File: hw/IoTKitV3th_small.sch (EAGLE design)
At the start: 13 parts

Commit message: Verdrated
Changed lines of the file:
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@@
 <?xml version="1.0" encoding="utf-8"?>
 <!DOCTYPE eagle SYSTEM "eagle.dtd">
-<eagle version="9.2.0">
+<eagle version="9.5.2">
 <drawing>
 <settings>
@@
 </plain>
 <instances>
-<instance part="B1" gate="G$1" x="22.86" y="38.1" rot="R90">
+<instance part="B1" gate="G$1" x="22.86" y="38.1" smashed="yes" rot="R90">
 <attribute name="NAME" x="2.286" y="28.448" size="1.778" layer="95" font="vector" rot="R90"/>
 <attribute name="VALUE" x="48.514" y="29.21" size="1.778" layer="96" font="vector" rot="R90" align="top-left"/>
 </instance>
-<instance part="H-BRIDGE" gate="G$1" x="144.78" y="40.64" rot="R90">
+<instance part="H-BRIDGE" gate="G$1" x="144.78" y="40.64" smashed="yes" rot="R90">
 <attribute name="NAME" x="123.444" y="30.48" size="1.778" layer="95" rot="R90"/>
 <attribute name="VALUE" x="167.64" y="30.48" size="1.778" layer="96" rot="R90"/>
 </instance>
-<instance part="M02" gate="G$1" x="147.32" y="71.12" rot="R90">
+<instance part="M02" gate="G$1" x="147.32" y="71.12" smashed="yes" rot="R90">
 <attribute name="NAME" x="141.605" y="64.77" size="1.778" layer="95" rot="R90"/>
 <attribute name="VALUE" x="152.4" y="64.77" size="1.778" layer="96" rot="R90"/>
 </instance>
-<instance part="M01" gate="G$1" x="144.78" y="10.16" rot="R270">
+<instance part="M01" gate="G$1" x="144.78" y="10.16" smashed="yes" rot="R270">
 <attribute name="NAME" x="150.495" y="16.51" size="1.778" layer="95" rot="R270"/>
 <attribute name="VALUE" x="139.7" y="16.51" size="1.778" layer="96" rot="R270"/>
 </instance>
-<instance part="SPI" gate="A" x="11.43" y="127" rot="R90">
+<instance part="SPI" gate="A" x="11.43" y="127" smashed="yes" rot="R90">
 <attribute name="NAME" x="0.635" y="120.65" size="1.778" layer="95" rot="R90"/>
 <attribute name="VALUE" x="21.59" y="120.65" size="1.778" layer="96" rot="R90"/>
 </instance>
-<instance part="NFC/RFID" gate="A" x="50.8" y="127" rot="R90">
+<instance part="NFC/RFID" gate="A" x="50.8" y="127" smashed="yes" rot="R90">
 <attribute name="NAME" x="37.465" y="120.65" size="1.778" layer="95" rot="R90"/>
 <attribute name="VALUE" x="63.5" y="120.65" size="1.778" layer="96" rot="R90"/>
 </instance>
-<instance part="HALL-SENSOR" gate="A" x="109.22" y="127" rot="R90">
+<instance part="HALL-SENSOR" gate="A" x="109.22" y="127" smashed="yes" rot="R90">
 <attribute name="NAME" x="103.505" y="120.65" size="1.778" layer="95" rot="R90"/>
 <attribute name="VALUE" x="116.84" y="120.65" size="1.778" layer="96" rot="R90"/>
 </instance>
-<instance part="OLED(0X78)" gate="A" x="147.32" y="127" rot="R90">
+<instance part="OLED(0X78)" gate="A" x="147.32" y="127" smashed="yes" rot="R90">
 <attribute name="NAME" x="139.065" y="120.65" size="1.778" layer="95" rot="R90"/>
 <attribute name="VALUE" x="154.94" y="120.65" size="1.778" layer="96" rot="R90"/>
 </instance>
-<instance part="SUPPLY2" gate="+5V" x="33.02" y="17.78" rot="R180">
+<instance part="SUPPLY2" gate="+5V" x="33.02" y="17.78" smashed="yes" rot="R180">
 <attribute name="VALUE" x="34.925" y="14.605" size="1.778" layer="96" rot="R180"/>
 </instance>
-<instance part="GND1" gate="1" x="43.18" y="20.32">
+<instance part="GND1" gate="1" x="43.18" y="20.32" smashed="yes">
 <attribute name="VALUE" x="40.64" y="17.78" size="1.778" layer="96"/>
 </instance>
-<instance part="GND3" gate="1" x="144.78" y="20.32">
+<instance part="GND3" gate="1" x="144.78" y="20.32" smashed="yes">
 <attribute name="VALUE" x="142.24" y="17.78" size="1.778" layer="96"/>
 </instance>
-<instance part="GND4" gate="1" x="144.78" y="60.96" rot="R180">
+<instance part="GND4" gate="1" x="144.78" y="60.96" smashed="yes" rot="R180">
 <attribute name="VALUE" x="147.32" y="63.5" size="1.778" layer="96" rot="R180"/>
 </instance>
-<instance part="GND8" gate="1" x="-8.382" y="66.548" rot="R270">
+<instance part="GND8" gate="1" x="-8.382" y="66.548" smashed="yes" rot="R270">
 <attribute name="VALUE" x="-10.922" y="69.088" size="1.778" layer="96" rot="R270"/>
 </instance>
-<instance part="SUPPLY4" gate="+5V" x="127" y="60.96">
+<instance part="SUPPLY4" gate="+5V" x="127" y="60.96" smashed="yes">
 <attribute name="VALUE" x="125.095" y="64.135" size="1.778" layer="96"/>
 </instance>
-<instance part="SUPPLY5" gate="+5V" x="162.56" y="17.78" rot="R180">
+<instance part="SUPPLY5" gate="+5V" x="162.56" y="17.78" smashed="yes" rot="R180">
 <attribute name="VALUE" x="164.465" y="14.605" size="1.778" layer="96" rot="R180"/>
 </instance>
-<instance part="SUPPLY9" gate="+5V" x="5.08" y="115.824" rot="R180">
+<instance part="SUPPLY9" gate="+5V" x="5.08" y="115.824" smashed="yes" rot="R180">
 <attribute name="VALUE" x="6.985" y="112.649" size="1.778" layer="96" rot="R180"/>
 </instance>
-<instance part="GND6" gate="1" x="0" y="114.3">
+<instance part="GND6" gate="1" x="0" y="114.3" smashed="yes">
 <attribute name="VALUE" x="-2.54" y="111.76" size="1.778" layer="96"/>
 </instance>
-<instance part="GND7" gate="1" x="142.24" y="111.76">
+<instance part="GND7" gate="1" x="142.24" y="111.76" smashed="yes">
 <attribute name="VALUE" x="139.7" y="109.22" size="1.778" layer="96"/>
 </instance>
-<instance part="SUPPLY10" gate="+5V" x="144.78" y="106.68" rot="R180">
+<instance part="SUPPLY10" gate="+5V" x="144.78" y="106.68" smashed="yes" rot="R180">
 <attribute name="VALUE" x="146.685" y="103.505" size="1.778" layer="96" rot="R180"/>
 </instance>
-<instance part="+3V1" gate="G$1" x="38.1" y="20.32" rot="R180"/>
-<instance part="+3V2" gate="G$1" x="58.42" y="114.3" rot="R180">
+<instance part="+3V1" gate="G$1" x="38.1" y="20.32" smashed="yes" rot="R180"/>
+<instance part="+3V2" gate="G$1" x="58.42" y="114.3" smashed="yes" rot="R180">
 <attribute name="VALUE" x="60.96" y="119.38" size="1.778" layer="96" rot="R270"/>
 </instance>
-<instance part="GND12" gate="1" x="53.34" y="114.3"/>
-<instance part="GND13" gate="1" x="109.22" y="137.16" rot="R180">
+<instance part="GND12" gate="1" x="53.34" y="114.3" smashed="yes"/>
+<instance part="GND13" gate="1" x="109.22" y="137.16" smashed="yes" rot="R180">
 <attribute name="VALUE" x="111.76" y="139.7" size="1.778" layer="96" rot="R180"/>
 </instance>
-<instance part="ESP8266" gate="A" x="-20.32" y="101.6">
+<instance part="ESP8266" gate="A" x="-20.32" y="101.6" smashed="yes">
 <attribute name="NAME" x="-26.67" y="109.855" size="1.778" layer="95"/>
 <attribute name="VALUE" x="-26.67" y="93.98" size="1.778" layer="96"/>
 </instance>
-<instance part="+3V4" gate="G$1" x="-7.62" y="116.84">
+<instance part="+3V4" gate="G$1" x="-7.62" y="116.84" smashed="yes">
 <attribute name="VALUE" x="-10.16" y="111.76" size="1.778" layer="96" rot="R90"/>
 </instance>
-<instance part="GND15" gate="1" x="-35.56" y="99.06" rot="R270">
+<instance part="GND15" gate="1" x="-35.56" y="99.06" smashed="yes" rot="R270">
 <attribute name="VALUE" x="-38.1" y="101.6" size="1.778" layer="96" rot="R270"/>
 </instance>
-<instance part="JP1" gate="A" x="-20.32" y="83.82">
+<instance part="JP1" gate="A" x="-20.32" y="83.82" smashed="yes">
 <attribute name="NAME" x="-26.67" y="89.535" size="1.778" layer="95"/>
 <attribute name="VALUE" x="-26.67" y="76.2" size="1.778" layer="96"/>
 </instance>
-<instance part="SD-CARD" gate="A" x="-19.05" y="132.08" rot="R90">
+<instance part="SD-CARD" gate="A" x="-19.05" y="132.08" smashed="yes" rot="R90">
 <attribute name="NAME" x="-16.51" y="135.255" size="1.778" layer="95" rot="R180"/>
 <attribute name="VALUE" x="-8.89" y="125.73" size="1.778" layer="96" rot="R90"/>
 </instance>
-<instance part="GND16" gate="1" x="-27.94" y="119.38">
+<instance part="GND16" gate="1" x="-27.94" y="119.38" smashed="yes">
 <attribute name="VALUE" x="-30.48" y="116.84" size="1.778" layer="96"/>
 </instance>
-<instance part="POTI" gate="1" x="-20.32" y="53.34">
+<instance part="POTI" gate="1" x="-20.32" y="53.34" smashed="yes">
 <attribute name="NAME" x="-26.289" y="49.53" size="1.778" layer="95" rot="R90"/>
 <attribute name="VALUE" x="-24.13" y="49.53" size="1.778" layer="96" rot="R90"/>
 </instance>
-<instance part="+3V3" gate="G$1" x="-20.32" y="40.64" rot="R180">
+<instance part="+3V3" gate="G$1" x="-20.32" y="40.64" smashed="yes" rot="R180">
 <attribute name="VALUE" x="-17.78" y="45.72" size="1.778" layer="96" rot="R270"/>
 </instance>
-<instance part="HUM/TEMP" gate="A" x="83.82" y="127" rot="R90">
+<instance part="HUM/TEMP" gate="A" x="83.82" y="127" smashed="yes" rot="R90">
 <attribute name="NAME" x="78.105" y="120.65" size="1.778" layer="95" rot="R90"/>
 <attribute name="VALUE" x="91.44" y="120.65" size="1.778" layer="96" rot="R90"/>

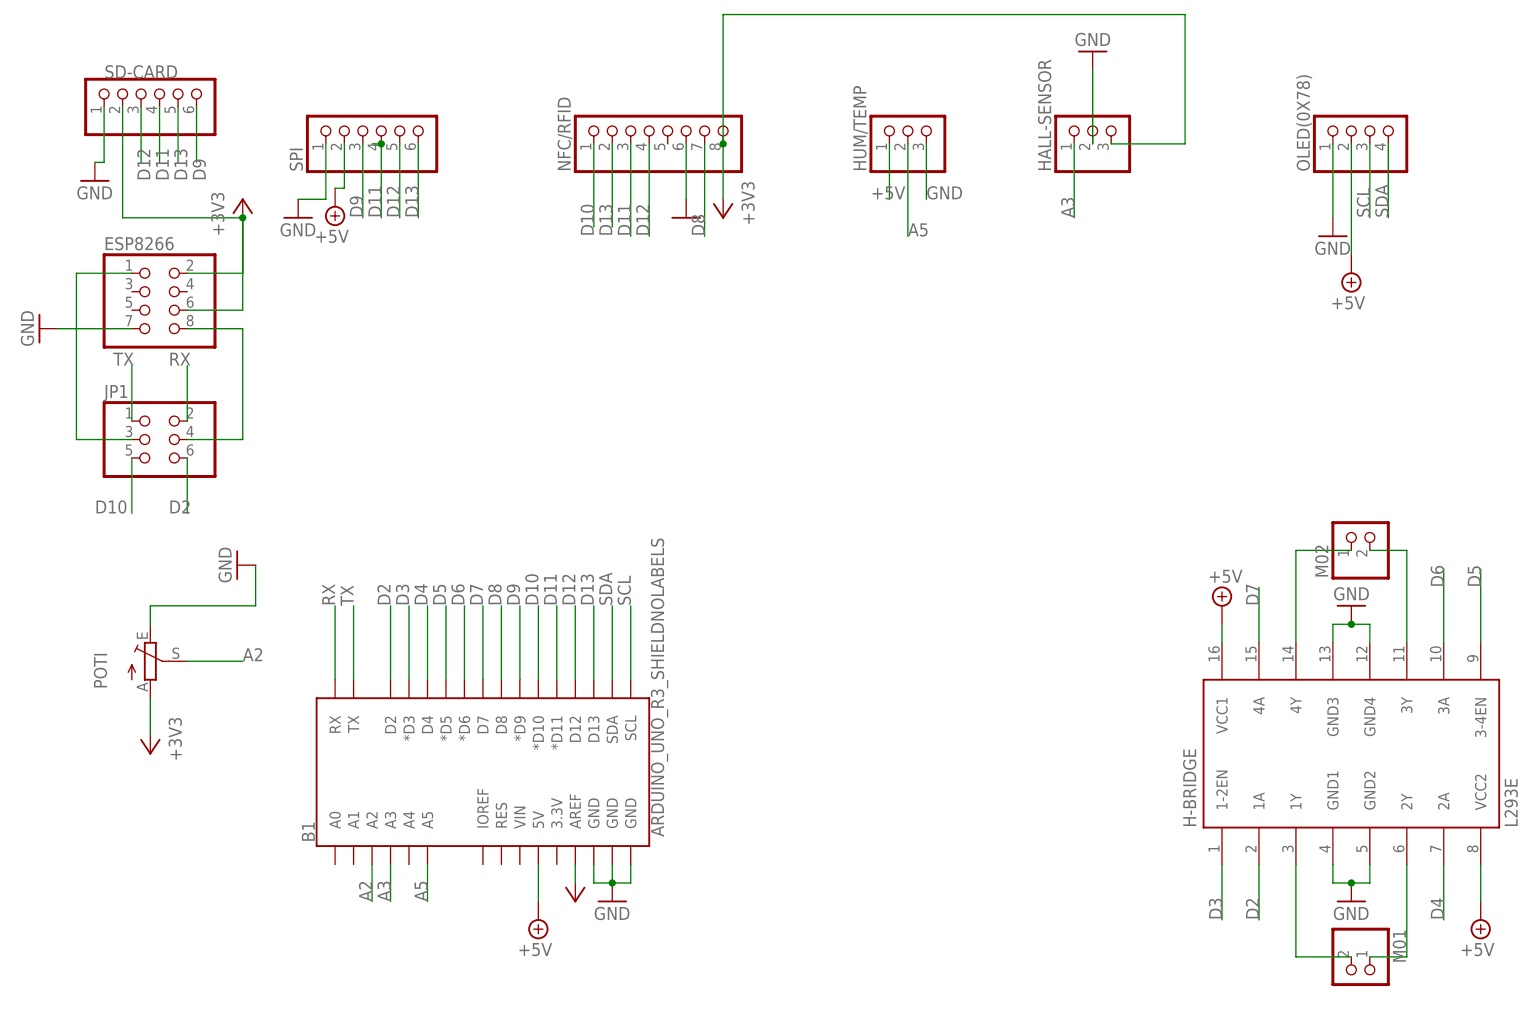
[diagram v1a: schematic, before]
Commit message: Grove und Servo Anschluesse
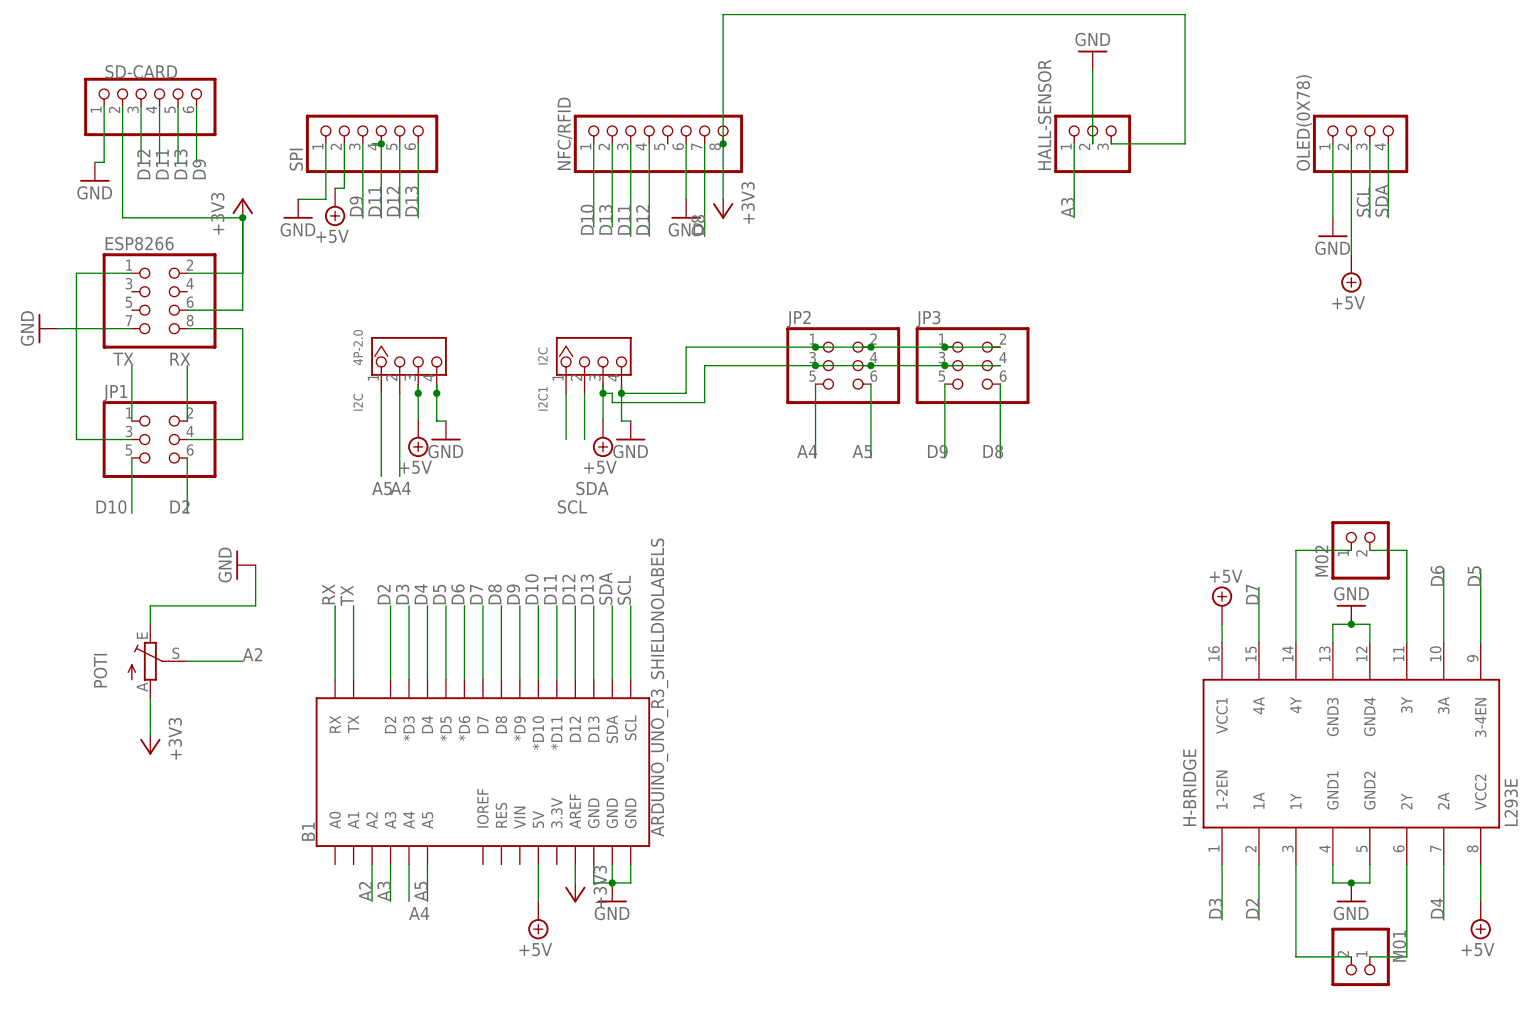
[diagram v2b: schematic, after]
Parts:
- removed HUM/TEMP: (no value), pinhead:PINHD-1X3
- added I2C: 4P-2.0, Seeed-Connector:GROVE-CONNECTOR-DIP(4P-2.0)
- added I2C1: I2C, Seeed-Connector:GROVE-CONNECTOR-DIP(4P-2.0)
- added JP2, JP3: (no value), pinhead:PINHD-2X3
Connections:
- new net A4: B1.A4, I2C.2, JP2.5
- net +5V: now also I2C.3, I2C1.3, JP2.3, JP2.4, JP3.3, JP3.4; no longer HUM/TEMP.1
- net A5: now also I2C.1, JP2.6; no longer HUM/TEMP.2
- net D8: now also JP3.6
- net D9: now also JP3.5
- net GND: now also I2C.4, I2C1.4, JP2.1, JP2.2, JP3.1, JP3.2; no longer HUM/TEMP.3
- net SCL: now also I2C1.1
- net SDA: now also I2C1.2

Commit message: R1.1
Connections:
- net A4: now also JP3.6; no longer JP2.5
- net A5: now also JP3.5; no longer JP2.6
- net D8: now also JP2.6; no longer JP3.6
- net D9: now also JP2.5; no longer JP3.5
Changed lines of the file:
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@@
 </segment>
 <segment>
-<pinref part="JP3" gate="A" pin="6"/>
-<wire x1="96.52" y1="91.44" x2="96.52" y2="81.28" width="0.1524" layer="91"/>
-<label x="93.98" y="81.28" size="1.778" layer="95"/>
+<pinref part="JP2" gate="A" pin="6"/>
+<wire x1="78.74" y1="91.44" x2="78.74" y2="81.28" width="0.1524" layer="91"/>
+<label x="76.2" y="81.28" size="1.778" layer="95"/>
 </segment>
 </net>
@@
 </segment>
 <segment>
-<pinref part="JP3" gate="A" pin="5"/>
-<wire x1="88.9" y1="91.44" x2="88.9" y2="81.28" width="0.1524" layer="91"/>
-<label x="86.36" y="81.28" size="1.778" layer="95"/>
+<pinref part="JP2" gate="A" pin="5"/>
+<wire x1="71.12" y1="91.44" x2="71.12" y2="81.28" width="0.1524" layer="91"/>
+<label x="68.58" y="81.28" size="1.778" layer="95"/>
 </segment>
 </net>
@@
 </segment>
 <segment>
-<pinref part="JP2" gate="A" pin="6"/>
-<wire x1="78.74" y1="91.44" x2="78.74" y2="81.28" width="0.1524" layer="91"/>
-<label x="76.2" y="81.28" size="1.778" layer="95"/>
+<pinref part="JP3" gate="A" pin="5"/>
+<wire x1="88.9" y1="91.44" x2="88.9" y2="81.28" width="0.1524" layer="91"/>
+<label x="86.36" y="81.28" size="1.778" layer="95"/>
 </segment>
 </net>
@@
 </segment>
 <segment>
-<pinref part="JP2" gate="A" pin="5"/>
-<wire x1="71.12" y1="91.44" x2="71.12" y2="81.28" width="0.1524" layer="91"/>
-<label x="68.58" y="81.28" size="1.778" layer="95"/>
-</segment>
-</net>
+<pinref part="JP3" gate="A" pin="6"/>
+<wire x1="96.52" y1="91.44" x2="96.52" y2="81.28" width="0.1524" layer="91"/>
+<label x="93.98" y="81.28" size="1.778" layer="95"/>
+</segment>
+</net>
